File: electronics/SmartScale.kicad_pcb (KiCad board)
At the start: 2 copper layers, 43.2 x 57.8 mm, 68 parts, among them IC1 HX711, J2 Conn_01x06, J3 Conn_01x06, J4 Conn_01x04, P1 USB_C_Plug_USB2.0, Q1 BC847, Q2 BC847, Q3 IRLML0030, Q4 IRLML0030, Q5 MMBT3906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

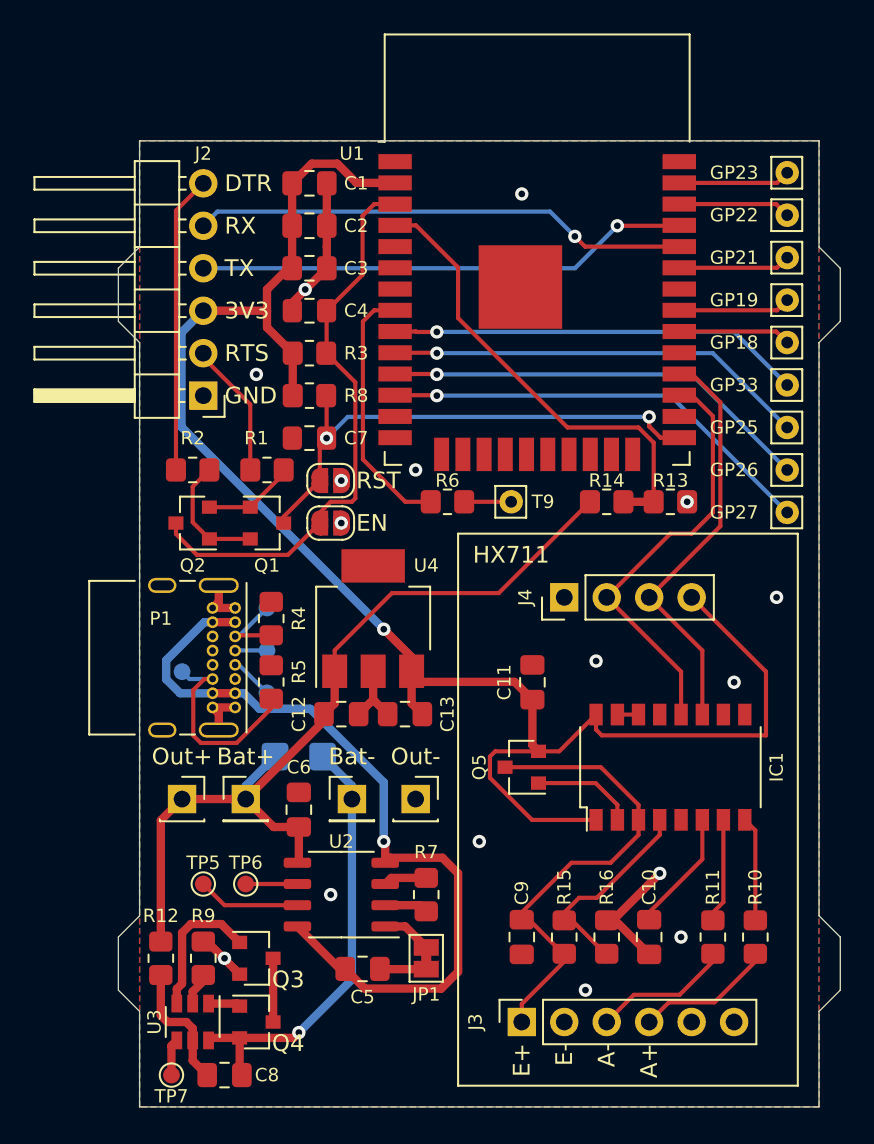
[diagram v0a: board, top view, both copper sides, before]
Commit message: Pushed casing and updated PCB
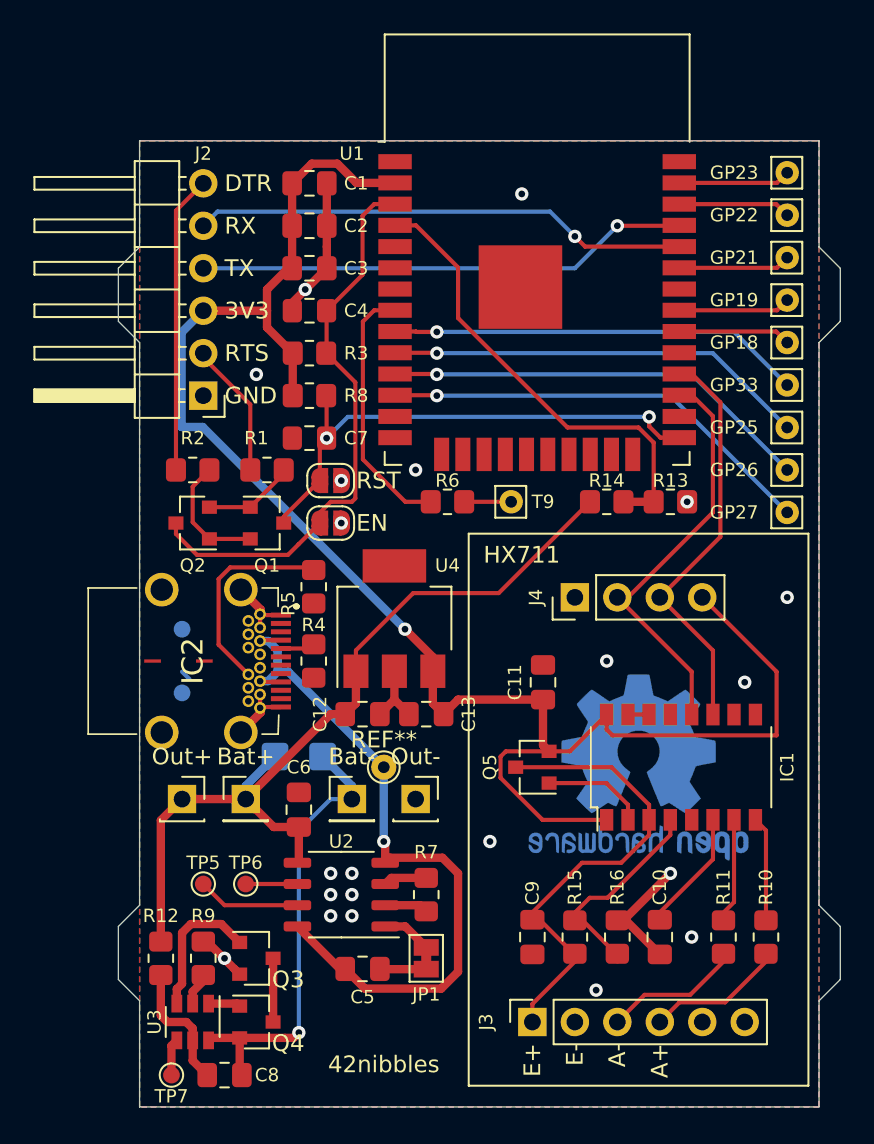
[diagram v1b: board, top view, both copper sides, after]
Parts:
- removed P1: USB_C_Plug_USB2.0, Connector_USB:USB_C_Receptacle_GCT_USB4085
- removed TP3, TP4: TestPoint, TestPoint:TestPoint_Pad_D1.0mm
- added IC2: 632723100011, Wuerth:632723100011, F.Cu at (142.9, 121.3)
- added REF**: TestPoint_THTPad_D1.5mm_Drill0.7mm, TestPoint:TestPoint_THTPad_D1.5mm_Drill0.7mm, F.Cu at (154.3, 127.6)
- added REF**: OSHW-Logo2_14.6x12mm_Copper, Symbol:OSHW-Logo2_14.6x12mm_Copper, B.Cu at (169.5, 127.6)
- moved R5 6.24 mm to (150.1, 116.8), turned to 90 degrees
- moved TP2 5.24 mm to (142.2, 119.4)
- moved TP1 5.08 mm to (142.2, 123.2)
- moved R4 3.59 mm to (150.1, 121.3)
- moved C12 1.27 mm to (153.0, 124.5)
- moved C13 1.27 mm to (156.8, 124.5)
- moved U4 1.27 mm to (154.9, 118.7)
- moved C11 0.64 mm to (163.8, 122.6)
- moved IC1 0.64 mm to (172.1, 127.6)
- moved J4 0.64 mm to (165.7, 117.5)
- moved R15 0.64 mm to (165.7, 137.8)
- moved R16 0.64 mm to (168.3, 137.8)
- moved C10 0.63 mm to (170.8, 137.8)
- moved C9 0.63 mm to (163.2, 137.8)
- moved J3 0.63 mm to (163.2, 142.9)
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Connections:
- R4 pad 1: GND -> Net-(IC2-PadA5)
- R4 pad 2: Net-(P1-PadA5) -> GND
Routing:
- net +5V: track 48.9 -> 43.2 mm
- net Net-(P1-PadA5): track 4.80 -> 0.00 mm
- net GND: track 36.1 -> 39.0 mm, vias 16 -> 21
- net Net-(IC2-PadA7): track 2.60 -> 0.00 mm
- net Net-(IC2-PadA5): track 0.00 -> 2.06 mm
- net Net-(IC2-PadA6): track 1.91 -> 0.00 mm
- net Net-(BAT2-Pad1): track 26.5 -> 27.2 mm
- net HX711_DOUT: track 25.6 -> 25.0 mm
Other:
- outline, holes or cut-outs redrawn
- board text added: "42nibbles"

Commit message: PCB Rev 5
- Added 42Nibbles QR Code
- Moved 5V connection
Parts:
- removed the REF** at (154.3, 127.6)
- removed the REF** at (169.5, 127.6)
- added 5V: TestPoint_THTPad_D1.5mm_Drill0.7mm, TestPoint:TestPoint_THTPad_D1.5mm_Drill0.7mm, F.Cu at (151.8, 142.9)
- added GND: TestPoint_THTPad_D1.5mm_Drill0.7mm, TestPoint:TestPoint_THTPad_D1.5mm_Drill0.7mm, F.Cu at (154.9, 142.9)
- added QR*****: Nibbler_Small, Nibbler:Nibbler_Small, B.Cu at (168.2, 128.3)
- added REF**: OSHW-Logo2_9.8x8mm_Copper, Symbol:OSHW-Logo2_9.8x8mm_Copper, B.Cu at (157.5, 137.2)
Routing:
- net +5V: track 43.2 -> 46.8 mm
- net GND: vias 21 -> 20
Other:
- board text added: "Rev. 05"

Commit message: Pushing changes made at my University
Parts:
- C10, C8: value 0.1uF -> 100nF
- C4, C7: footprint Capacitor_SMD:C_0805_2012Metric_Pad1.15x1.40mm_HandSolder -> Capacitor_SMD:C_0805_2012Metric_Pad1.18x1.45mm_HandSolder
- R4, R5: value 5.1 -> 5.1k
- R7: value R -> 12k
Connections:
- IC1 pad 13: (no net) -> unconnected-(IC1-Pad13)
- IC2 pad A10: (no net) -> unconnected-(IC2-PadA10)
- IC2 pad A11: (no net) -> unconnected-(IC2-PadA11)
- IC2 pad A2: (no net) -> unconnected-(IC2-PadA2)
- IC2 pad A3: (no net) -> unconnected-(IC2-PadA3)
- IC2 pad A8: (no net) -> unconnected-(IC2-PadA8)
- IC2 pad B10: (no net) -> unconnected-(IC2-PadB10)
- IC2 pad B11: (no net) -> unconnected-(IC2-PadB11)
- IC2 pad B2: (no net) -> unconnected-(IC2-PadB2)
- IC2 pad B3: (no net) -> unconnected-(IC2-PadB3)
- IC2 pad B6: (no net) -> unconnected-(IC2-PadB6)
- IC2 pad B7: (no net) -> unconnected-(IC2-PadB7)
- IC2 pad B8: (no net) -> unconnected-(IC2-PadB8)
- J3 pad 5: (no net) -> unconnected-(J3-Pad5)
- J3 pad 6: (no net) -> unconnected-(J3-Pad6)
- U1 pad 13: (no net) -> unconnected-(U1-Pad13)
- U1 pad 14: (no net) -> unconnected-(U1-Pad14)
- U1 pad 16: (no net) -> unconnected-(U1-Pad16)
- U1 pad 17: (no net) -> unconnected-(U1-Pad17)
- U1 pad 18: (no net) -> unconnected-(U1-Pad18)
- U1 pad 19: (no net) -> unconnected-(U1-Pad19)
- U1 pad 20: (no net) -> unconnected-(U1-Pad20)
- U1 pad 21: (no net) -> unconnected-(U1-Pad21)
- U1 pad 22: (no net) -> unconnected-(U1-Pad22)
- U1 pad 23: (no net) -> unconnected-(U1-Pad23)
- U1 pad 24: (no net) -> unconnected-(U1-Pad24)
- U1 pad 26: (no net) -> unconnected-(U1-Pad26)
- U1 pad 29: (no net) -> unconnected-(U1-Pad29)
- U1 pad 32: (no net) -> unconnected-(U1-Pad32)
- U1 pad 5: (no net) -> unconnected-(U1-Pad5)
- U1 pad 6: (no net) -> unconnected-(U1-Pad6)
- U1 pad 7: (no net) -> unconnected-(U1-Pad7)
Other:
- net class Default removed

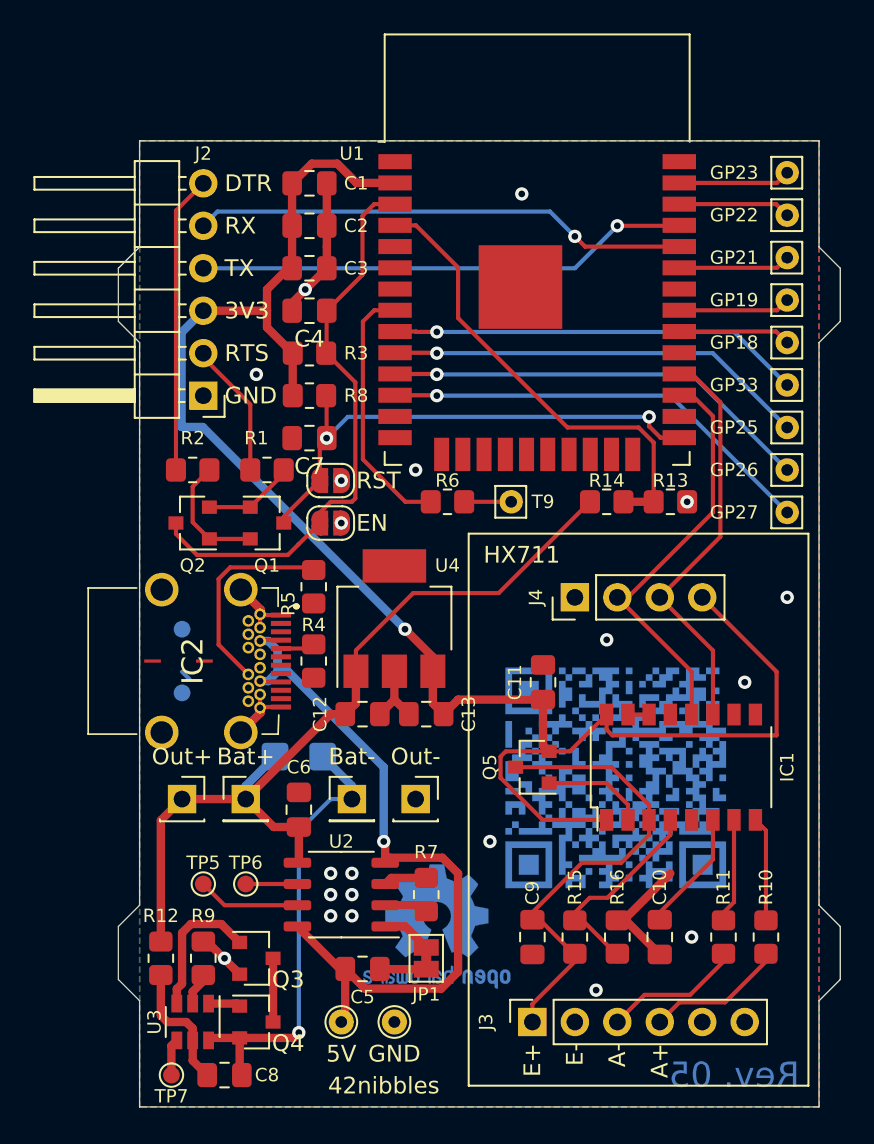
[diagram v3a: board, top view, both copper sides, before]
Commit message: PCB Rev 6, fixed error with flashing
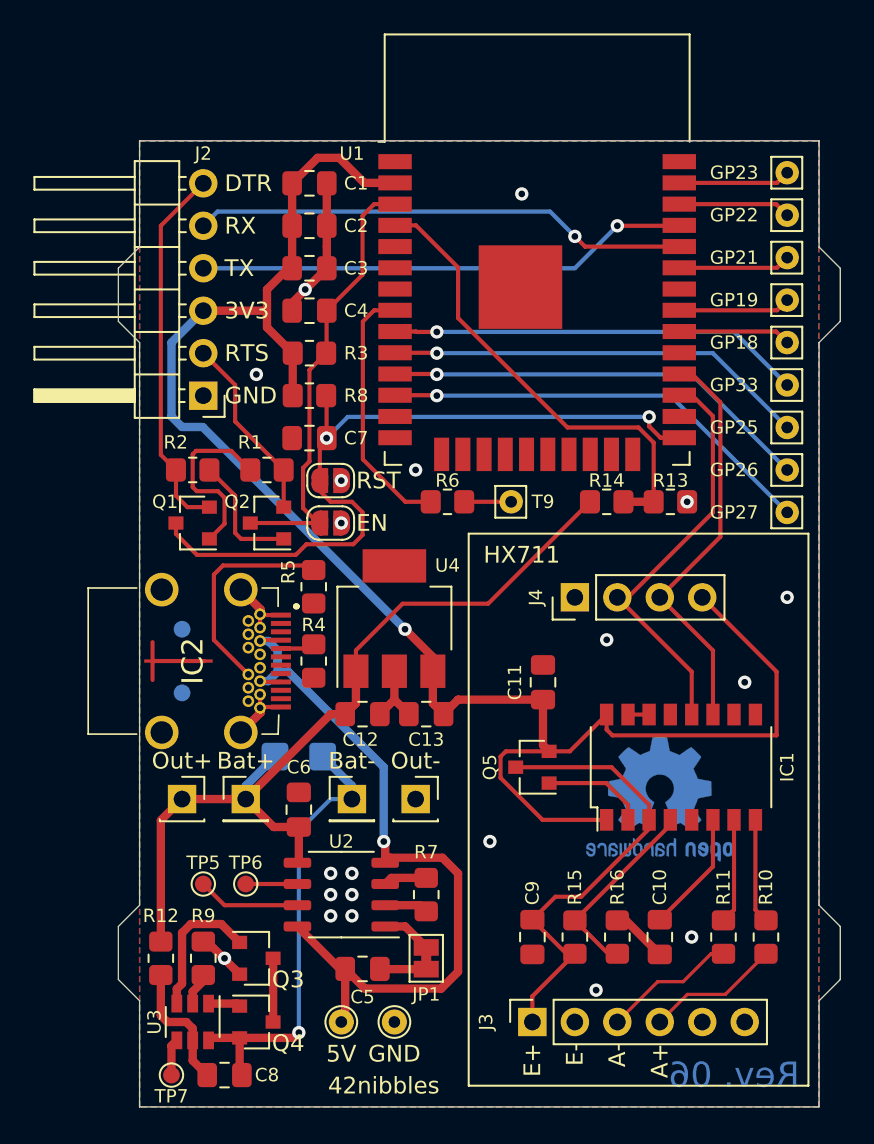
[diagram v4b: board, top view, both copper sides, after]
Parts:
- removed QR*****: Nibbler_Small, Nibbler:Nibbler_Small
- moved REF** 15.4 mm to (170.8, 129.5)
- moved Q1 4.44 mm to (142.9, 113.0), turned to 180 degrees
- moved Q2 4.44 mm to (147.3, 113.0)
- turned R1 to 0 degrees
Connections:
- Q1 pad 2: Net-(Q1-Pad2) -> /DTR
- Q2 pad 1: Net-(Q1-Pad2) -> Net-(Q2-Pad1)
- Q2 pad 2: Net-(Q1-Pad1) -> /RTS
- R2 pad 1: Net-(Q1-Pad2) -> Net-(Q2-Pad1)
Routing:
- net ESP32_RST: track 31.2 -> 45.6 mm
- net ESP32_EN: track 34.4 -> 26.8 mm
- net Net-(Q2-Pad1): track 0.00 -> 7.46 mm
- net Net-(Q1-Pad2): track 7.40 -> 0.00 mm
- net Net-(Q1-Pad1): track 5.50 -> 11.0 mm
- net /DTR: track 17.8 -> 22.4 mm
- net /RTS: track 8.15 -> 11.2 mm
- net Net-(IC1-Pad4): track 12.5 -> 11.7 mm
- net GND: track 39.0 -> 39.7 mm
- net Net-(IC2-PadB5): track 12.5 -> 13.1 mm
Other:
- board text added: "Rev. 06"
- board text removed: "Rev. 05"
